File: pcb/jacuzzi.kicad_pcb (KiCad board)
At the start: 2 copper layers, 144 x 100 mm, 79 parts, among them J1 Conn_01x03, J10 Conn_01x02, J11 Conn_01x03, J13 Conn_01x01, J14 Conn_01x01, J15 Conn_01x01, J16 Conn_01x01, J2 Conn_01x03, J3 Conn_01x03, J4 Conn_01x05, J5 Conn_01x03, J6 Conn_01x03, J7 Conn_01x02, J8 Conn_01x08, J9 USB_C_Receptacle_PowerOnly_6P, K1 G5LE-1, Q1 MMBT3904, Q2 MMBT3904, Q3 MMBT3904, Q4 IRF4905STRLPBF, Q5 MMBT3904, Q6 IRF4905STRLPBF, U1 LM2575-3.3BU, U2 LM2575-5.0BU, U3 ESP32-DEVKITC-32U, U4 DM-OLED096-636

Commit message: started layout
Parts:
- J4: footprint Connector_JST:JST_SH_BM04B-SRSS-TB_1x04-1MP_P1.00mm_Vertical -> Connector_JST:JST_SH_SM04B-SRSS-TB_1x04-1MP_P1.00mm_Horizontal
- moved J4 25.8 mm to (139.0, 52.0), turned to 180 degrees
- moved R9 7.47 mm to (146.0, 62.0)
- moved R10 7.35 mm to (146.0, 59.0)
- moved D9 3.61 mm to (146.0, 55.0), turned to 180 degrees
- moved J15 3.50 mm to (206.6, 109.0)
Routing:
- net GND: track 0.00 -> 667.6 mm, vias 0 -> 1
- net +5V: track 0.00 -> 268.7 mm, vias 0 -> 3
- net +3.3V: track 0.00 -> 232.3 mm, vias 0 -> 4
- net VS: track 0.00 -> 135.8 mm, vias 0 -> 1
- net /GPIO_Servo: track 0.00 -> 85.6 mm
- net /GPIO_Dallas2: track 0.00 -> 77.4 mm
- net /GPIO_TubValve: track 0.00 -> 76.0 mm
- net /GPIO_ADC7: track 0.00 -> 73.9 mm
- net /GPIO_I2C_SDA: track 0.00 -> 71.2 mm
- net /GPIO_BallValveOpen_Feedback: track 0.00 -> 69.6 mm
- net /GPIO_Dallas1: track 0.00 -> 68.8 mm
- net /GPIO_I2C_SCL: track 0.00 -> 67.6 mm, vias 0 -> 1
- net /GPIO_ADC8: track 0.00 -> 64.9 mm, vias 0 -> 1
- net /GPIO_BallValveClose_Feedback: track 0.00 -> 55.7 mm
- net /GPIO_BallValveOpen: track 0.00 -> 49.2 mm, vias 0 -> 1
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
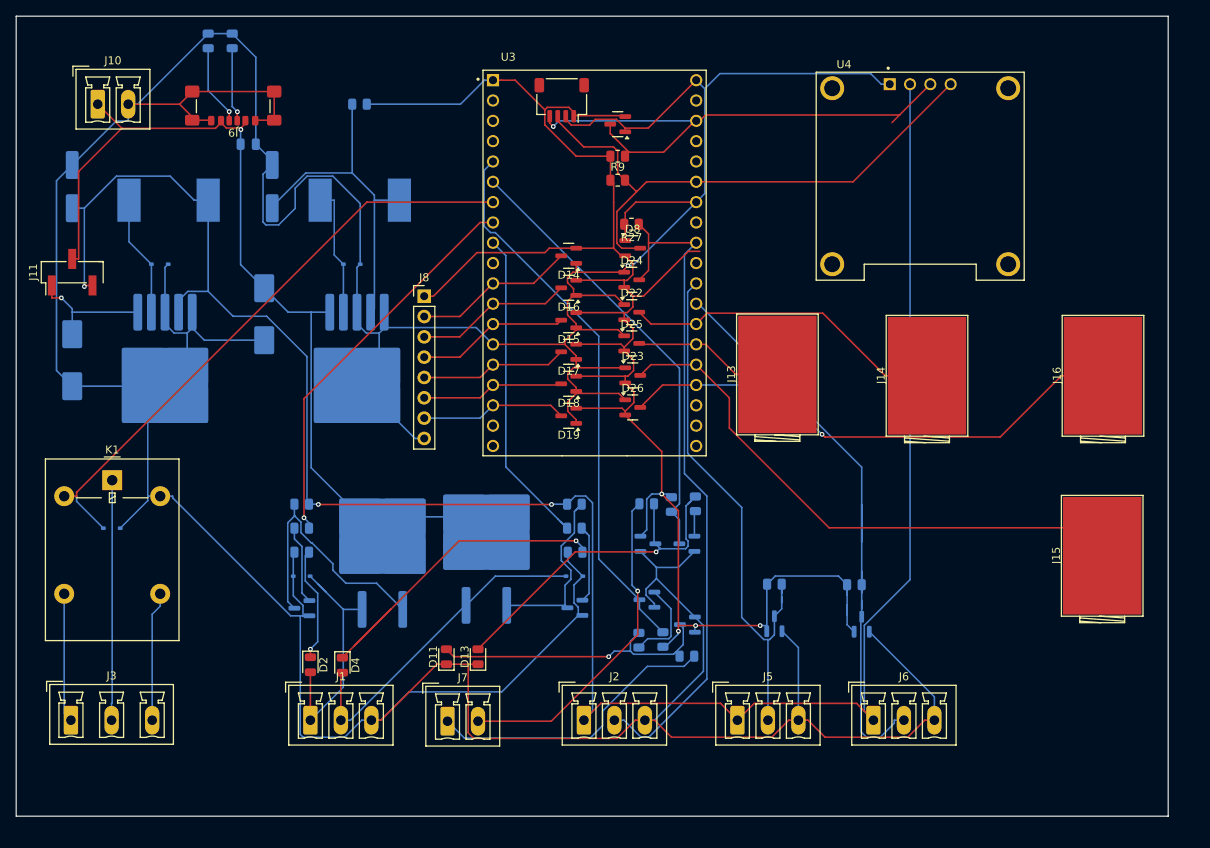
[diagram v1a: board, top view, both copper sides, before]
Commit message: started on bom
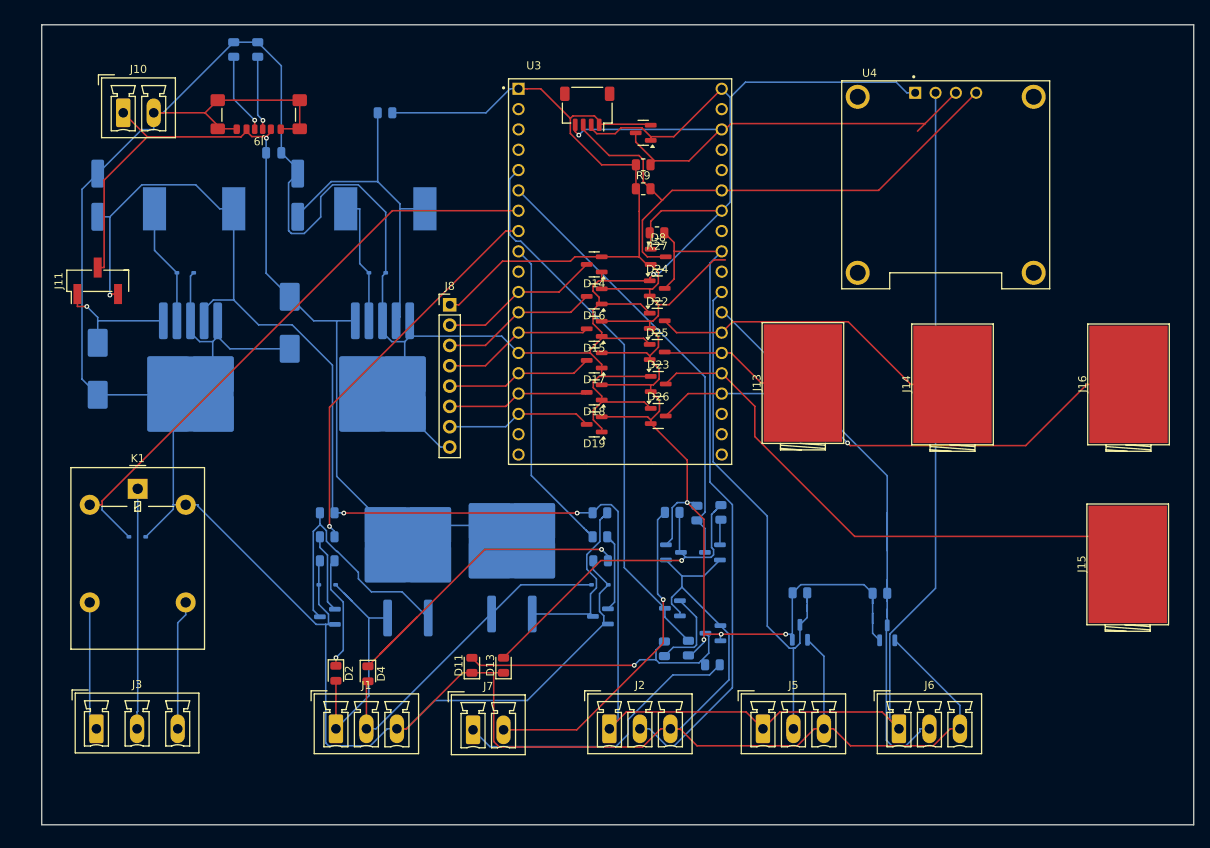
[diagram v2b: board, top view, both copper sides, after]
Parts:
- moved D11 3.37 mm to (127.8, 122.6)
- moved D2 3.37 mm to (110.8, 123.6)
- moved D4 3.37 mm to (114.8, 123.7)
- moved Q3 3.37 mm to (109.7, 116.6)
- moved Q4 3.37 mm to (119.8, 109.1)
- moved J1 3.37 mm to (110.8, 130.6)
- moved J7 3.37 mm to (127.9, 130.7)
- moved C1 3.37 mm to (103.0, 58.6)
- moved C2 3.37 mm to (105.0, 79.8)
- moved C3 3.37 mm to (106.0, 63.9)
- moved C4 3.37 mm to (81.0, 85.6)
- moved C5 3.37 mm to (81.0, 63.9)
- moved D1 3.37 mm to (109.7, 112.6)
- moved D10 3.37 mm to (157.9, 118.6)
- moved D12 3.37 mm to (153.0, 108.5)
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
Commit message: cleanup on pcb and added grapics. need to make a logo
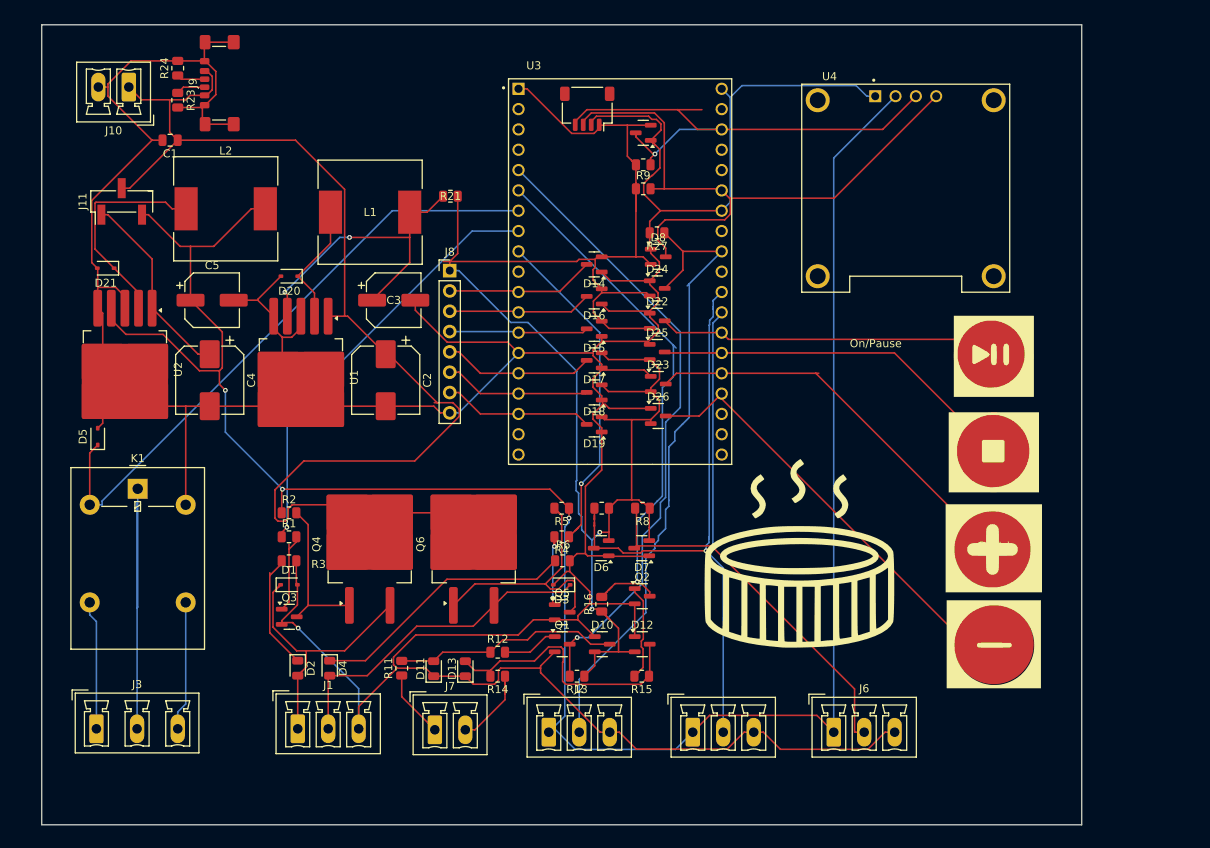
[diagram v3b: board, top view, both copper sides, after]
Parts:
- removed J13, J14, J15, J16: Conn_01x01, Connector:IHI_B6A-PCB-45_Vertical
- added G***: LOGO, LOGO, F.Cu at (193.0, 96.0)
- added G***: LOGO, LOGO, F.Cu at (169.0, 109.0)
- added G***: LOGO, LOGO, F.Cu at (193.0, 84.0)
- added G***: LOGO, LOGO, F.Cu at (193.0, 120.0)
- added G***: LOGO, LOGO, F.Cu at (193.0, 108.0)
- added TP1: TestPoint, TestPoint:TestPoint_Pad_D4.0mm, F.Cu at (193.0, 120.0)
- added TP2: TestPoint, TestPoint:TestPoint_Pad_D4.0mm, F.Cu at (193.0, 96.0)
- added TP3: TestPoint, TestPoint:TestPoint_Pad_D4.0mm, F.Cu at (193.0, 84.0)
- added TP4: TestPoint, TestPoint:TestPoint_Pad_D4.0mm, F.Cu at (193.0, 108.0)
- C1, C2, C3, C4, C5, D1, D10, D12, D20, D21, D3, D5, D6, D7, L1, L2, Q1, Q2, Q3, Q4, Q5, Q6, R1, R11, R12, R13, R14, R15, R16, R2, R21, R23, R24, R3, R4, R5, R6, R7, R8, U1, U2: moved to F.Cu
- moved R11 38.8 mm to (119.0, 123.0), turned to 90 degrees
- moved D7 32.5 mm to (149.0, 108.0), turned to 180 degrees
- moved R8 31.5 mm to (149.1, 103.0), turned to 180 degrees
- moved R14 29.9 mm to (131.0, 124.0), turned to 180 degrees
- moved D6 27.0 mm to (143.9, 108.0), turned to 180 degrees
- moved R7 26.9 mm to (144.0, 103.0), turned to 180 degrees
- moved R15 22.7 mm to (149.0, 124.0), turned to 180 degrees
- moved R12 20.8 mm to (131.0, 121.0), turned to 0 degrees
- moved C5 19.4 mm to (95.3, 77.0), turned to 0 degrees
- moved C3 17.8 mm to (118.0, 77.0), turned to 0 degrees
- moved R16 16.5 mm to (144.0, 115.0), turned to 90 degrees
- moved Q1 14.5 mm to (139.1, 120.0), turned to 0 degrees
- moved R13 14.4 mm to (140.9, 124.0), turned to 180 degrees
- moved C4 14.1 mm to (95.0, 87.0)
- moved C2 14.0 mm to (117.0, 87.0)
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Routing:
- net GND: track 667.6 -> 544.7 mm
- net VS: track 135.8 -> 169.1 mm, vias 1 -> 0
- net /BallValveClose_Feedback: track 41.5 -> 10.6 mm, vias 1 -> 0
- net /BallValveOpen_Feedback: track 37.0 -> 8.50 mm
- net /GPIO_ADC6: track 18.9 -> 46.3 mm
- net /GPIO_ADC7: track 73.9 -> 51.0 mm
- net Net-(Q3-C): track 33.3 -> 19.4 mm
- net /TubValve_V: track 30.0 -> 43.3 mm
- net Net-(D4-K): track 45.7 -> 33.3 mm, vias 1 -> 0
- net /GPIO_BallValveClose_Feedback: track 55.7 -> 68.1 mm, vias 0 -> 1
- net Net-(D21-K): track 15.2 -> 27.2 mm
- net Net-(D12-COM): track 44.7 -> 34.5 mm, vias 1 -> 0
- net Net-(Q2-B): track 3.19 -> 13.2 mm
- net Net-(Q5-C): track 22.5 -> 32.3 mm
- net /GPIO_ADC8: track 64.9 -> 55.3 mm, vias 1 -> 0
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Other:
- board size 144 x 100 mm -> 130 x 100 mm
- board text added: "On/Pause"

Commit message: add diode for 3v and 5v, missing markings on pcb
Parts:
- removed TP1, TP2, TP3, TP4: TestPoint, TestPoint:TestPoint_Pad_D4.0mm
- added D27: 5V, LED_SMD:LED_0805_2012Metric, F.Cu at (108.0, 45.6)
- added D28: 3.3V, LED_SMD:LED_0805_2012Metric, F.Cu at (113.5, 45.6)
- added R17: 300R, Resistor_SMD:R_0805_2012Metric, F.Cu at (108.0, 49.9)
- added R18: 300R, Resistor_SMD:R_0805_2012Metric, F.Cu at (113.5, 50.1)

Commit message: add transistor to drive 5v on relay
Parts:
- added Q7: MMBT3904, Package_TO_SOT_SMD:SOT-23, F.Cu at (97.4, 101.5)
- added R19: 1K, Resistor_SMD:R_0805_2012Metric, F.Cu at (97.6, 105.5)
- J4: value Conn_01x05 -> Conn_02x02_Counter_Clockwise_MountingPin
- moved J4 0.20 mm to (142.0, 53.0)
- renumbered G*** to J13, G*** to J14, G*** to J15, G*** to J16
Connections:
- D5 pad 1: /GPIO_TubValve -> +5V
- D5 pad 2: GND -> Net-(D5-A)
- J4 pad MP: (no net) -> GND
- K1 pad 2: /GPIO_TubValve -> +5V
- K1 pad 5: GND -> Net-(D5-A)
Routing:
- net /GPIO_TubValve: track 77.0 -> 0.00 mm
- net GND: track 544.7 -> 532.3 mm

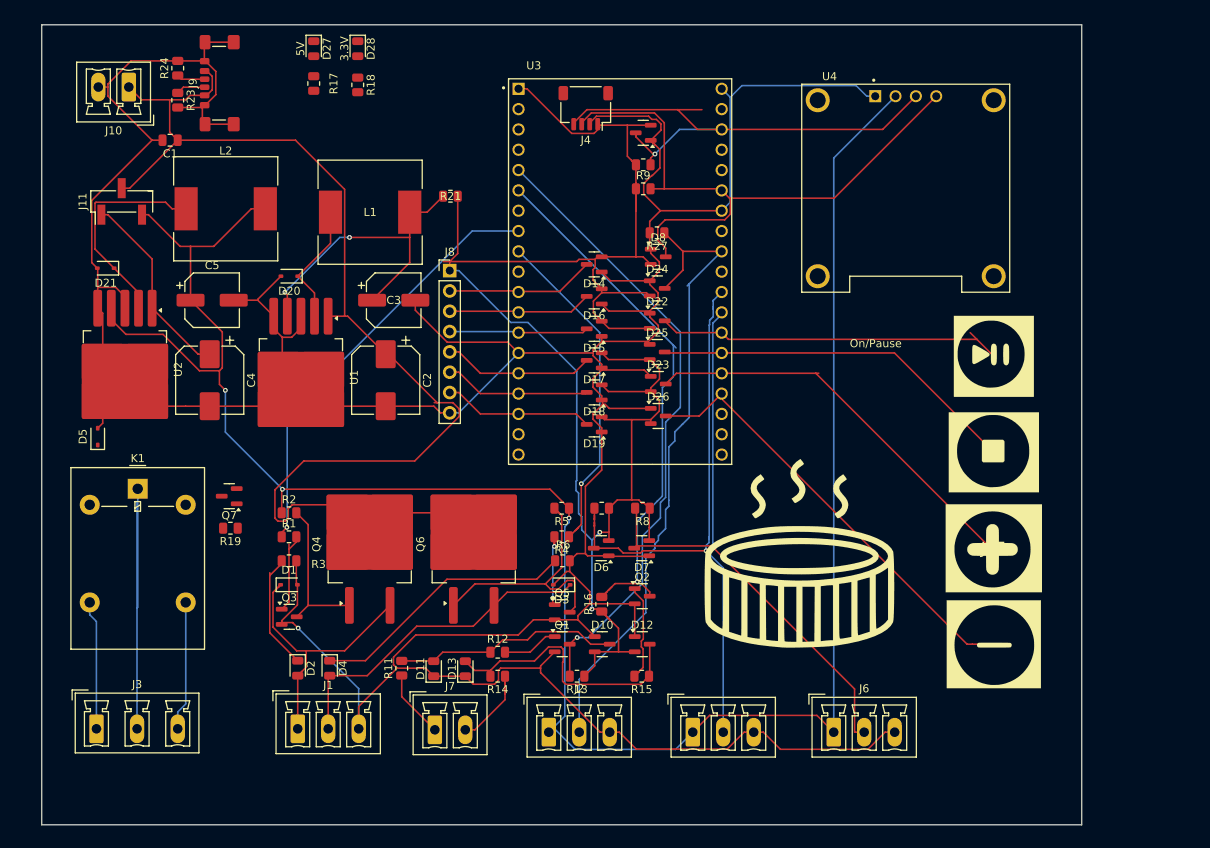
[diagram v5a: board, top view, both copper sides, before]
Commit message: now with all parts defined
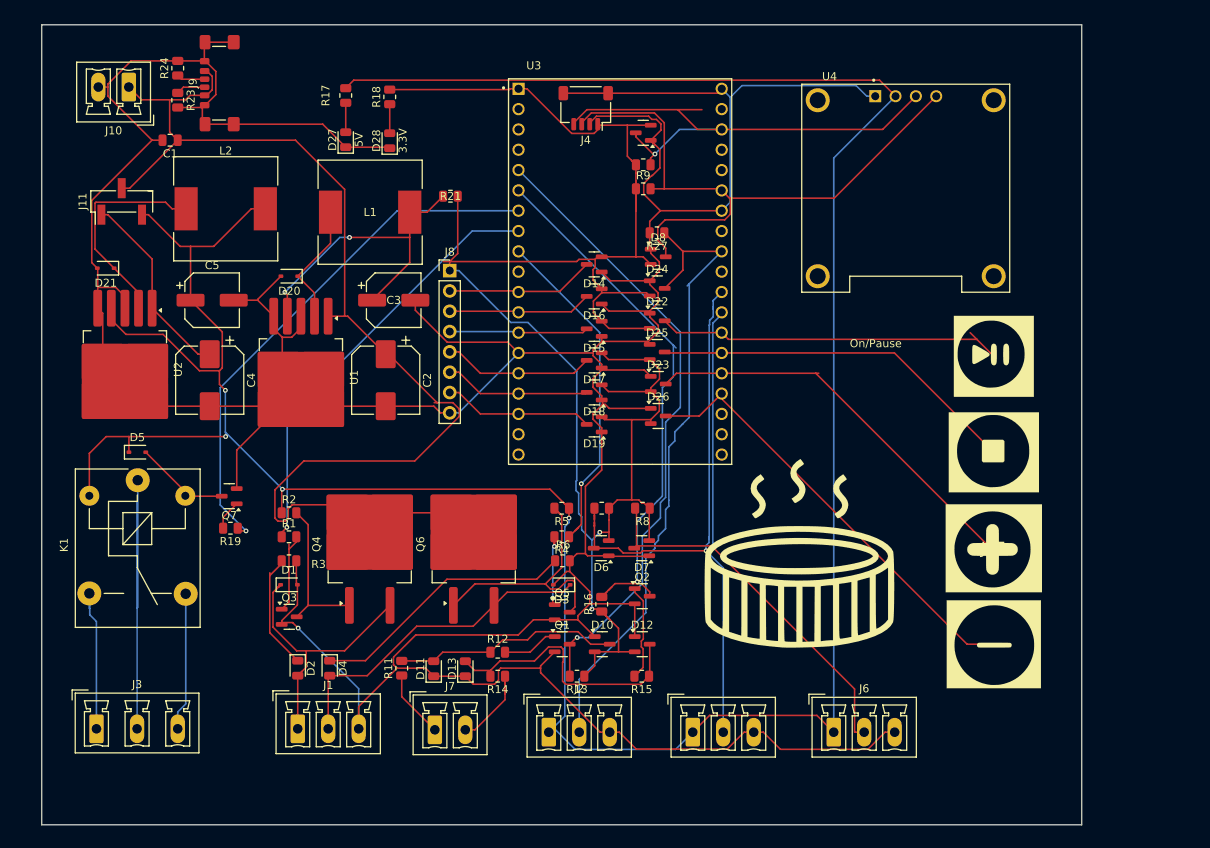
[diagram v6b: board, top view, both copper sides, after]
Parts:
- K1: value G5LE-1 -> SRD-05VDC; footprint Relay_THT:Relay_SPDT_Omron-G5LE-1 -> Relay_THT:Relay_SPDT_SANYOU_SRD_Series_Form_C
- moved D28 12.2 mm to (117.5, 57.1), turned to 90 degrees
- moved D27 12.1 mm to (112.0, 56.9), turned to 90 degrees
- moved D5 5.32 mm to (86.0, 96.0), turned to 0 degrees
- moved R17 4.27 mm to (112.0, 51.4), turned to 90 degrees
- moved R18 4.27 mm to (117.5, 51.6), turned to 90 degrees
- moved K1 1.08 mm to (86.0, 99.5), turned to -90 degrees
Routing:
- net +5V: track 263.4 -> 359.9 mm, vias 3 -> 4
- net /GPIO_TubValve: track 0.00 -> 66.9 mm, vias 0 -> 1
- net GND: track 532.3 -> 581.9 mm
- net +3.3V: track 223.1 -> 241.1 mm
- net Net-(D5-A): track 0.00 -> 12.1 mm
- net Net-(Q7-B): track 0.00 -> 3.75 mm
- net Net-(D27-A): track 0.00 -> 3.67 mm
- net Net-(D28-A): track 0.00 -> 3.62 mm
- net /TubValve_NO: track 16.1 -> 18.1 mm
- net /TubValve_V: track 43.3 -> 44.3 mm
- net /TubValve_NC: track 16.2 -> 17.3 mm

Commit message: ordered
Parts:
- added J12: Conn_01x03, Connector_Phoenix_MC:PhoenixContact_MCV_1,5_3-G-3.81_1x03_P3.81mm_Vertical, F.Cu at (155.7, 116.1)
- added J19: Conn_01x03, Connector_Phoenix_MC:PhoenixContact_MCV_1,5_3-G-3.81_1x03_P3.81mm_Vertical, F.Cu at (173.0, 116.0)
- added R20: 3K3, Resistor_SMD:R_0805_2012Metric, F.Cu at (155.5, 100.5)
- added R22: 3K3, Resistor_SMD:R_0805_2012Metric, F.Cu at (155.5, 104.5)
- added TP1: TestPoint, TestPoint:TestPoint_Pad_D4.0mm, F.Cu at (174.0, 87.8)
- added TP2: TestPoint, TestPoint:TestPoint_Pad_D4.0mm, F.Cu at (194.6, 88.0)
- added TP3: TestPoint, TestPoint:TestPoint_Pad_D4.0mm, F.Cu at (195.0, 105.0)
- added TP4: TestPoint, TestPoint:TestPoint_Pad_D4.0mm, F.Cu at (195.1, 120.4)
- J8: value Conn_01x08 -> Conn_01x06; footprint Connector_PinHeader_2.54mm:PinHeader_1x08_P2.54mm_Vertical -> Connector_PinHeader_2.54mm:PinHeader_1x06_P2.54mm_Vertical
- moved R23 39.5 mm to (129.0, 62.9)
- moved R24 38.0 mm to (126.0, 62.9), turned to -90 degrees
- moved D28 31.7 mm to (86.0, 61.0), turned to -90 degrees
- moved D27 31.3 mm to (81.0, 61.0), turned to -90 degrees
- moved R18 30.9 mm to (88.0, 60.9)
- moved R17 30.5 mm to (83.0, 61.0)
- moved J9 29.1 mm to (126.5, 51.5), turned to -90 degrees
- moved R19 22.3 mm to (118.0, 96.5), turned to -90 degrees
- moved J13 21.0 mm to (173.6, 88.0)
- moved Q7 15.8 mm to (112.6, 97.0)
- moved D5 15.2 mm to (100.5, 100.5), turned to 180 degrees
- moved G*** 8.32 mm to (173.5, 102.0)
- moved R4 7.70 mm to (143.0, 100.0)
- moved D14 7.53 mm to (143.0, 65.0)
- moved D16 6.53 mm to (143.1, 70.0)
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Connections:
- C2 pad 1: VS -> +5V
- D2 pad 1: Net-(D2-K) -> GND
- D2 pad 2: /BallValveOpen -> Net-(D2-A)
- D4 pad 1: Net-(D4-K) -> GND
- D4 pad 2: /BallValveClose -> Net-(D4-A)
- J8 pad 6: /GPIO9 -> GND
- Q4 pad 2: VS -> /BallValveOpen
- Q4 pad 3: /BallValveOpen -> VS
- Q6 pad 2: VS -> /BallValveClose
- Q6 pad 3: /BallValveClose -> VS
- R3 pad 1: Net-(D2-K) -> /BallValveOpen
- R3 pad 2: GND -> Net-(D2-A)
- R6 pad 1: Net-(D4-K) -> /BallValveClose
- R6 pad 2: GND -> Net-(D4-A)
- U1 pad 1: VS -> +5V
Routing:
- net /GPIO9: track 18.3 -> 61.4 mm, vias 0 -> 3
- net /GPIO10: track 18.8 -> 59.0 mm
- net +3.3V: track 241.1 -> 280.2 mm, vias 2 -> 4
- net Net-(D4-A): track 0.00 -> 38.9 mm, vias 0 -> 2
- net +5V: track 359.9 -> 323.3 mm, vias 4 -> 1
- net /GPIO_BallValveClose_Feedback: track 68.4 -> 103.4 mm
- net Net-(D4-K): track 33.3 -> 0.00 mm
- net /GPIO_TubValve: track 66.9 -> 43.3 mm
- net /GPIO_ADC6: track 46.3 -> 24.4 mm
- net VS: track 169.1 -> 147.4 mm, vias 0 -> 2
- net /BallValveClose: track 41.5 -> 61.6 mm
- net Net-(D2-A): track 0.00 -> 17.5 mm, vias 0 -> 2
- net GND: track 581.9 -> 598.8 mm, vias 1 -> 31
- net Net-(D2-K): track 14.9 -> 0.00 mm
- net /GPIO_BallValveOpen: track 53.9 -> 67.3 mm
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- added copper zone on B.Cu, net GND
- added copper zone on F.Cu, net GND
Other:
- board text added: "3V"
- board text added: "5V"
- board text added: "AIR TEMP"
- board text added: "CLOSE"
- board text added: "DRAIN TEMP"
- board text added: "GND"
- board text added: "GND 7-24V"
- board text added: "LINE"
- board text added: "MIXER TEMP"
- board text added: "NO 24V NC"
- board text added: "OPEN"
- board text added: "PWM"
- board text added: "SENSE"
- board text added: "THERMOSTAT"
- board text added: "TUB TEMP"
- board text added: "WATER IN"
- board text added: "WATER OUT"
- board text removed: "On/Pause"
